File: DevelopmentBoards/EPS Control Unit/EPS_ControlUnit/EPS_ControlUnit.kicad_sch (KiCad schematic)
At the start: 30 parts, among them J1 Conn_01x04_Pin, J2 USB_B_Micro, SW1 SW_SPDT, U1 STM32L476VET6, U2 AMS1117-3.3, Y1 32MHz

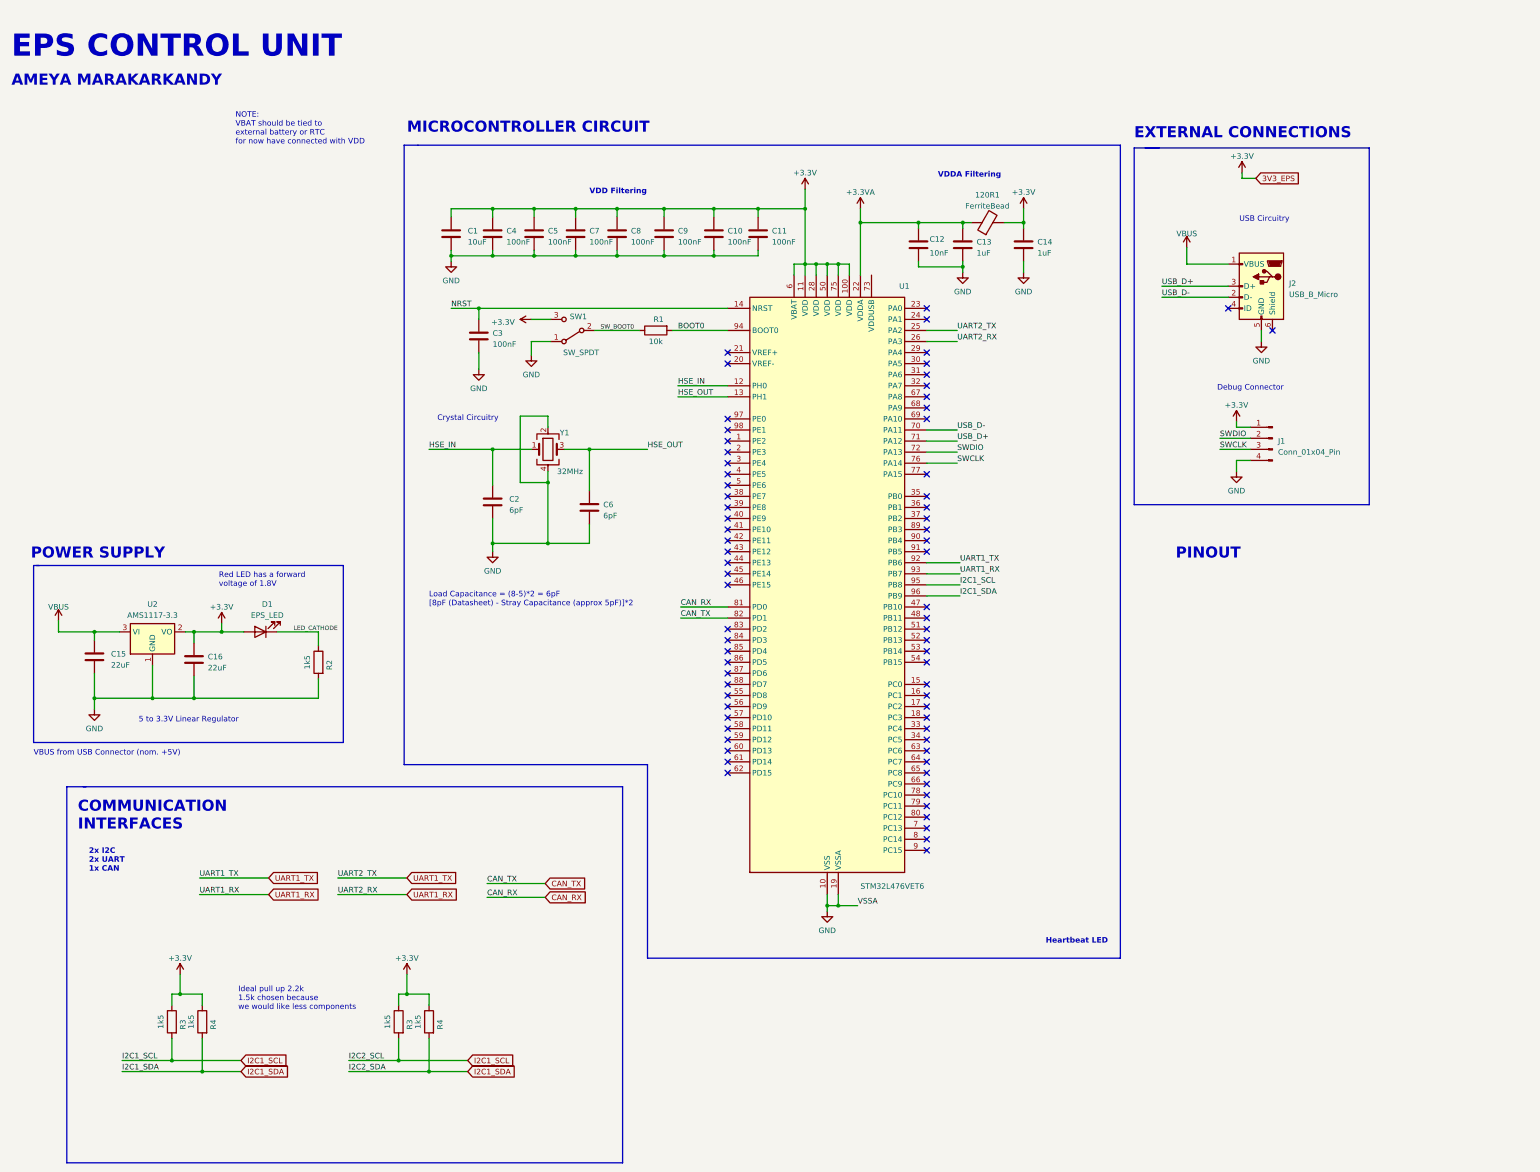
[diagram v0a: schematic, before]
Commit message: EPS Control Unit Dev Board development
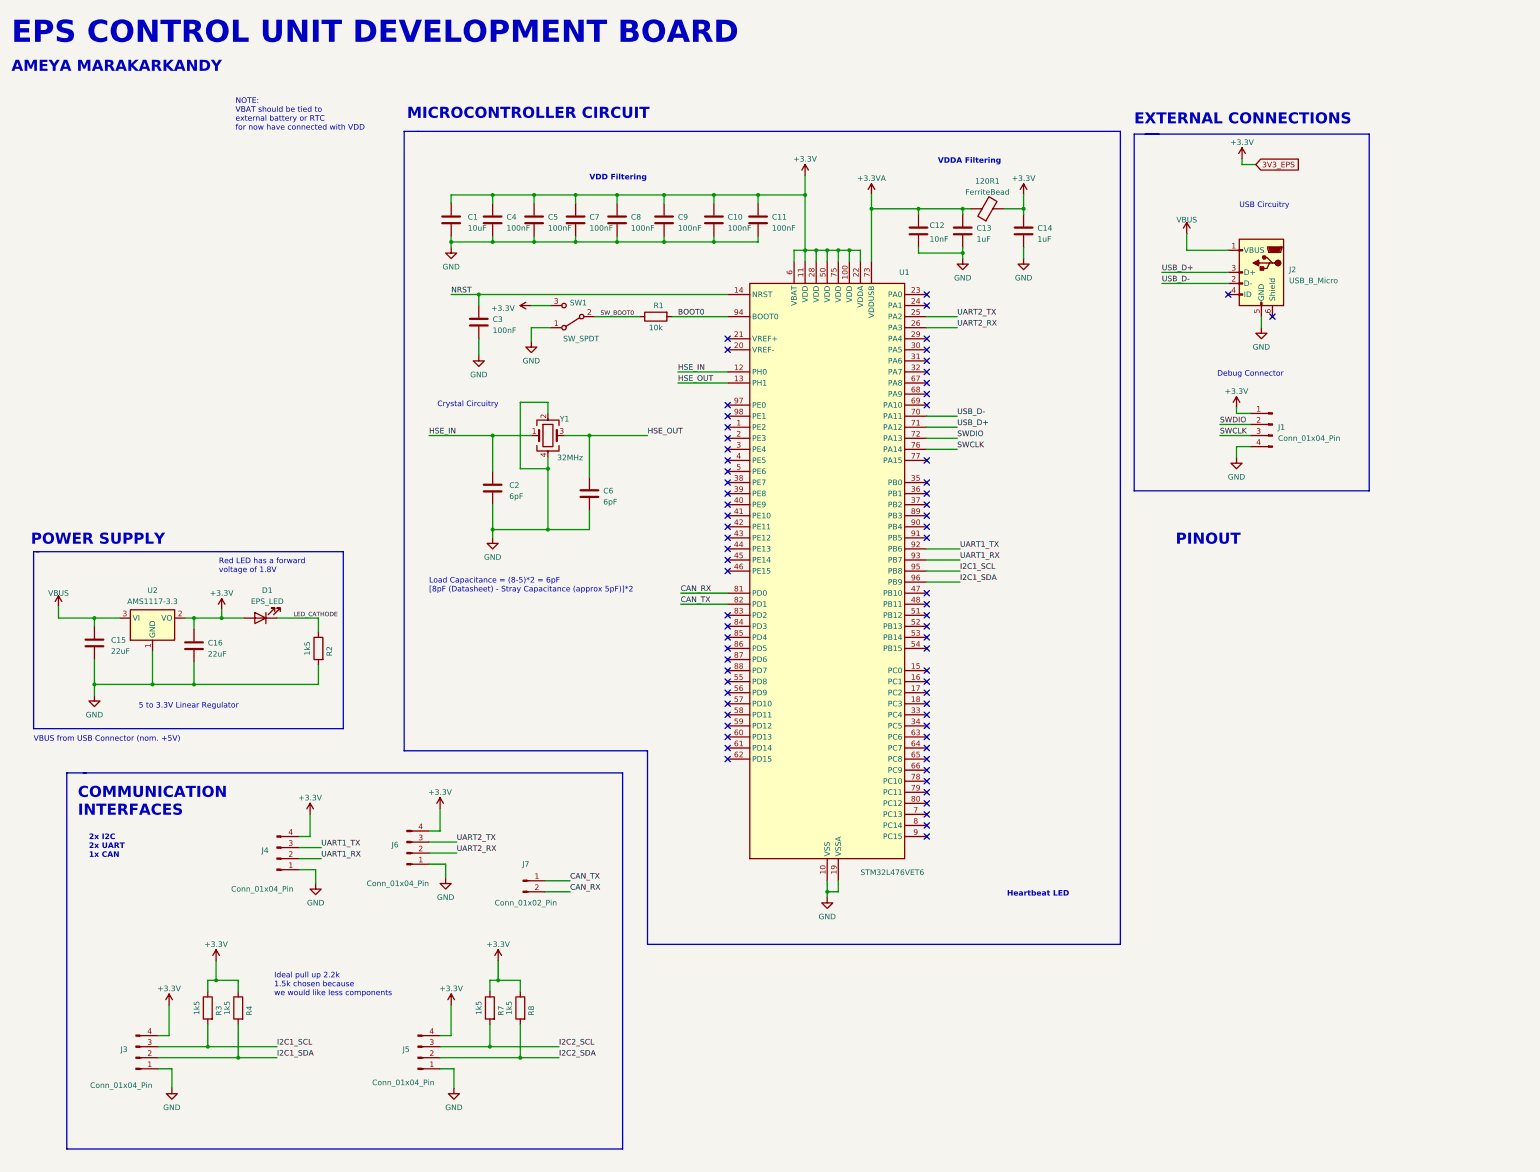
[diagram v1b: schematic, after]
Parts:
- removed R3 (x2), R4 (x2): 1k5, symbol Device:R
- added J3, J4, J5, J6: Conn_01x04_Pin, symbol Connector:Conn_01x04_Pin
- added J7: Conn_01x02_Pin, symbol Connector:Conn_01x02_Pin
- added R3, R4, R7, R8: 1k5, symbol Device:R
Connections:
- net +3.3V: now also U1.22 (VDDA), J3.4 (Pin_4), J4.4 (Pin_4), J5.4 (Pin_4), J6.4 (Pin_4), R3.1, R4.1, R7.1, R8.1
- net +3.3VA: now also U1.73 (VDDUSB); no longer U1.22 (VDDA)
- net CAN_RX: now also J7.2 (Pin_2)
- net CAN_TX: now also J7.1 (Pin_1)
- net GND: now also J3.1 (Pin_1), J4.1 (Pin_1), J5.1 (Pin_1), J6.1 (Pin_1)
- net I2C1_SCL: now also J3.3 (Pin_3), R3.2
- net I2C1_SDA: now also J3.2 (Pin_2), R4.2
- net UART1_RX: now also J4.2 (Pin_2); no longer U1.26 (PA3)
- net UART1_TX: now also J4.3 (Pin_3); no longer U1.25 (PA2)
- new net I2C2_SCL: J5.3 (Pin_3), R7.2
- new net I2C2_SDA: J5.2 (Pin_2), R8.2
- new net UART2_RX: J6.2 (Pin_2), U1.26 (PA3)
- new net UART2_TX: J6.3 (Pin_3), U1.25 (PA2)
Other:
- note added: "EPS CONTROL UNIT DEVELOPMENT BOARD"
- note removed: "EPS CONTROL UNIT"
- company: IIT Bombay Student Satellite Program -> IIT BOMBAY STUDENT SATELLITE PROGRAM
- title: EPS Control Unit -> EPS CONTROL UNIT DEV BOARD

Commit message: EPS Control Unit Rough layout done
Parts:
- added H1, H2, H3, H4: MountingHole_Pad, MountingHole:MountingHole_2.2mm_M2_Pad, symbol Mechanical:MountingHole_Pad
- added JP1, JP2: Jumper_2_Bridged, TestPoint:TestPoint_2Pads_Pitch2.54mm_Drill0.8mm, symbol Jumper:Jumper_2_Bridged
- added TP1, TP3, TP5, TP7, TP9: TestPoint, TestPoint:TestPoint_Pad_D1.0mm, symbol Connector:TestPoint
- added TP2, TP4, TP6, TP8: TestPoint, TestPoint:TestPoint_Pad_1.0x1.0mm, symbol Connector:TestPoint
- added U3: TPS3824-33QDBVRQ1, TPS3824:tps3824, symbol TPS3824:TPS3824-33QDBVRQ1
- 120R1: footprint (none) -> Inductor_SMD:L_0805_2012Metric
- C1, C10, C11, C12, C13, C14, C15, C16, C3, C4, C5, C7, C8, C9: footprint (none) -> Capacitor_SMD:C_0603_1608Metric
- C2, C6: value 6pF -> 10pF; footprint (none) -> Capacitor_SMD:C_0603_1608Metric
- D1: footprint (none) -> LED_SMD:LED_0805_2012Metric
- J1: footprint (none) -> Connector_PinHeader_2.54mm:PinHeader_1x04_P2.54mm_Vertical
- J2: footprint (none) -> Connector_USB:USB_Micro-B_GCT_USB3076-30-A
- J3, J4, J5, J6: footprint (none) -> Connector_PinSocket_2.54mm:PinSocket_1x04_P2.54mm_Vertical
- J7: footprint (none) -> Connector_PinSocket_2.54mm:PinSocket_1x02_P2.54mm_Vertical
- R1, R2, R3, R4, R7, R8: footprint (none) -> Resistor_SMD:R_0805_2012Metric
- SW1: footprint (none) -> Connector_PinHeader_2.54mm:PinHeader_1x03_P2.54mm_Vertical
- Y1: footprint (none) -> Crystal:Crystal_SMD_Abracon_ABM8AIG-4Pin_3.2x2.5mm
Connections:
- net +3.3V: now also U1.73 (VDDUSB), JP2.2 (B), TP7.1, U3.5 (VDD); no longer C16.1, U1.22 (VDDA), U2.2 (VO)
- net +3.3VA: now also U1.22 (VDDA), TP5.1; no longer U1.73 (VDDUSB)
- net GND: now also H1.1, H2.1, H3.1, H4.1, TP2.1, TP4.1, TP6.1, TP8.1, U3.2 (GND)
- net I2C2_SCL: now also U1.47 (PB10)
- net I2C2_SDA: now also U1.48 (PB11)
- net NRST: now also JP1.2 (B), TP9.1
- net VBUS: now also TP1.1
- net WDI: now reaches U1.57 (PD10)
- net WDI: now also U3.4 (WDI)
- new net 3V3_LDO: C16.1, JP2.1 (A), TP3.1, U2.2 (VO)
- new net WDI_RESET: JP1.1 (A), U3.3 (RESET)
- no-connect marks 72 -> 70
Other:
- note added: "Bulk capacitance"
- note added: "Load Capacitance = (10-5)*2 = 10pF [10pF (Datasheet) - Stray Capacitance (approx 5pF)]*2"
- note added: "M2"
- note added: "MOUNTING HOLES"
- note added: "REMINDER TO ADD EPS LED CONTROLLED BBY GPIO PIN"
- note added: "WATCHDOG TIMER"
- note removed: "Load Capacitance = (8-5)*2 = 6pF [8pF (Datasheet) - Stray Capacitance (approx 5pF)]*2"
- moved on the sheet: 120R1, C1, C10, C11, C12, C13, C14, C15, C16, C2, C3, C4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

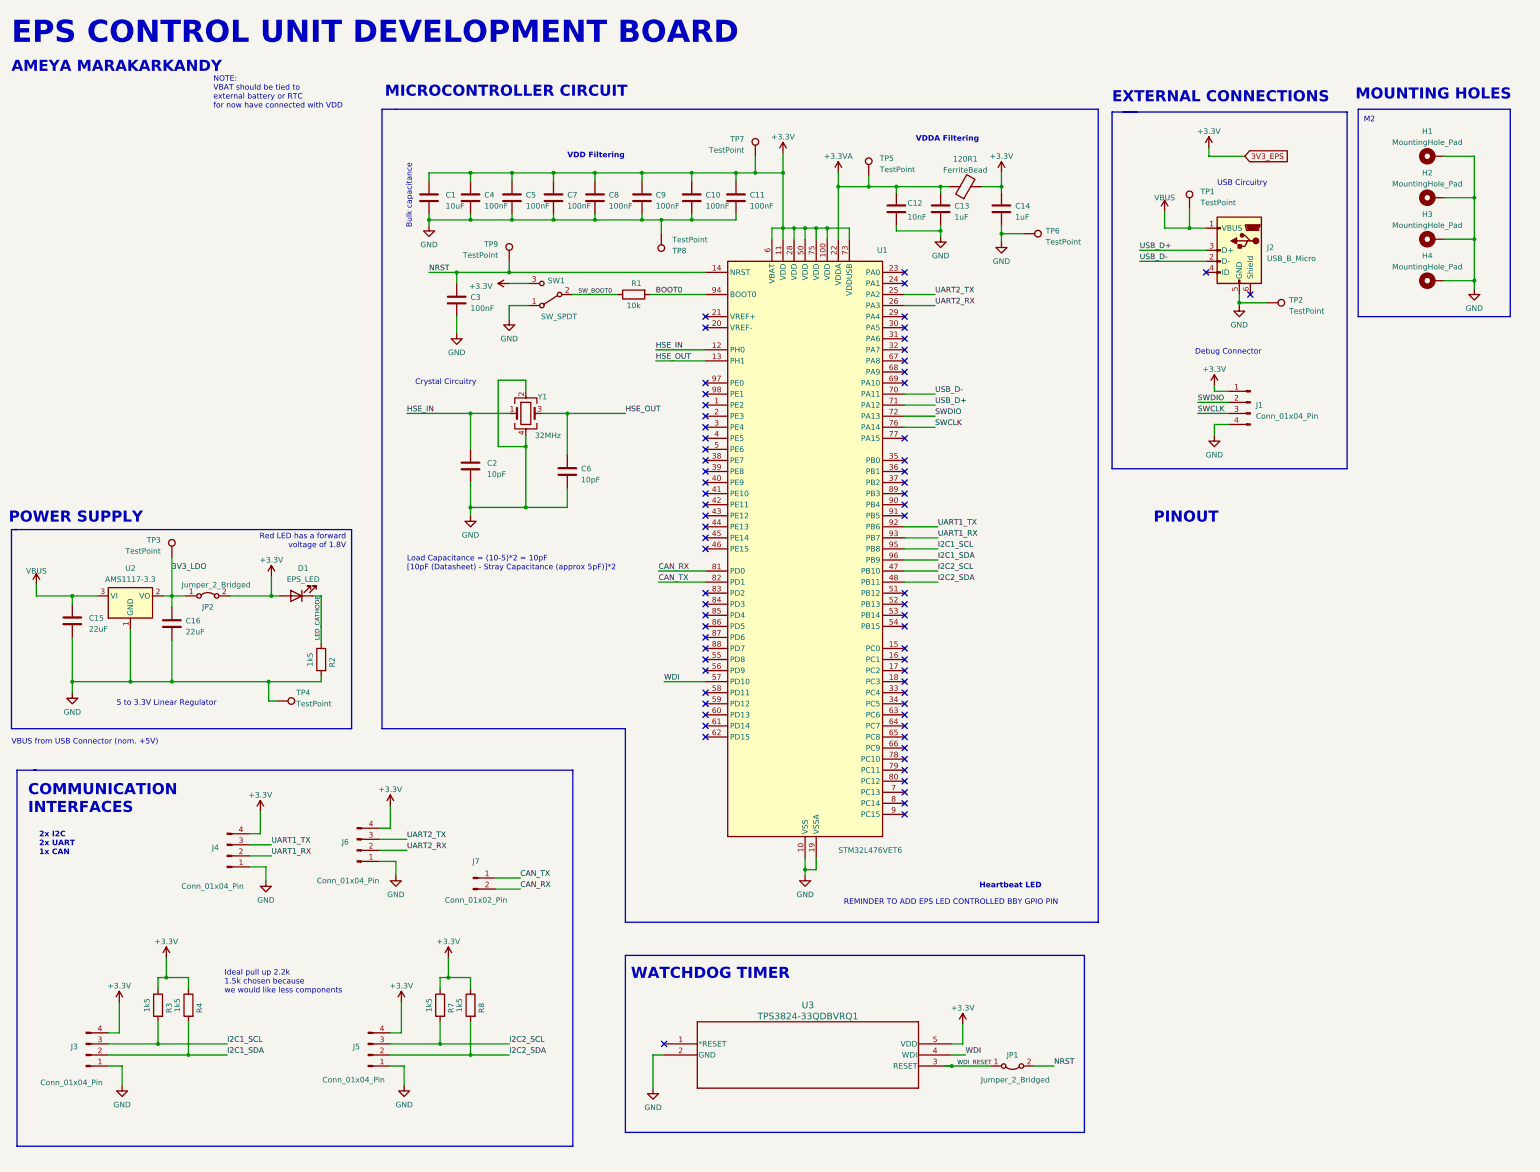
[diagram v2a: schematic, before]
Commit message: EPS Control Unit Dev Board Completed
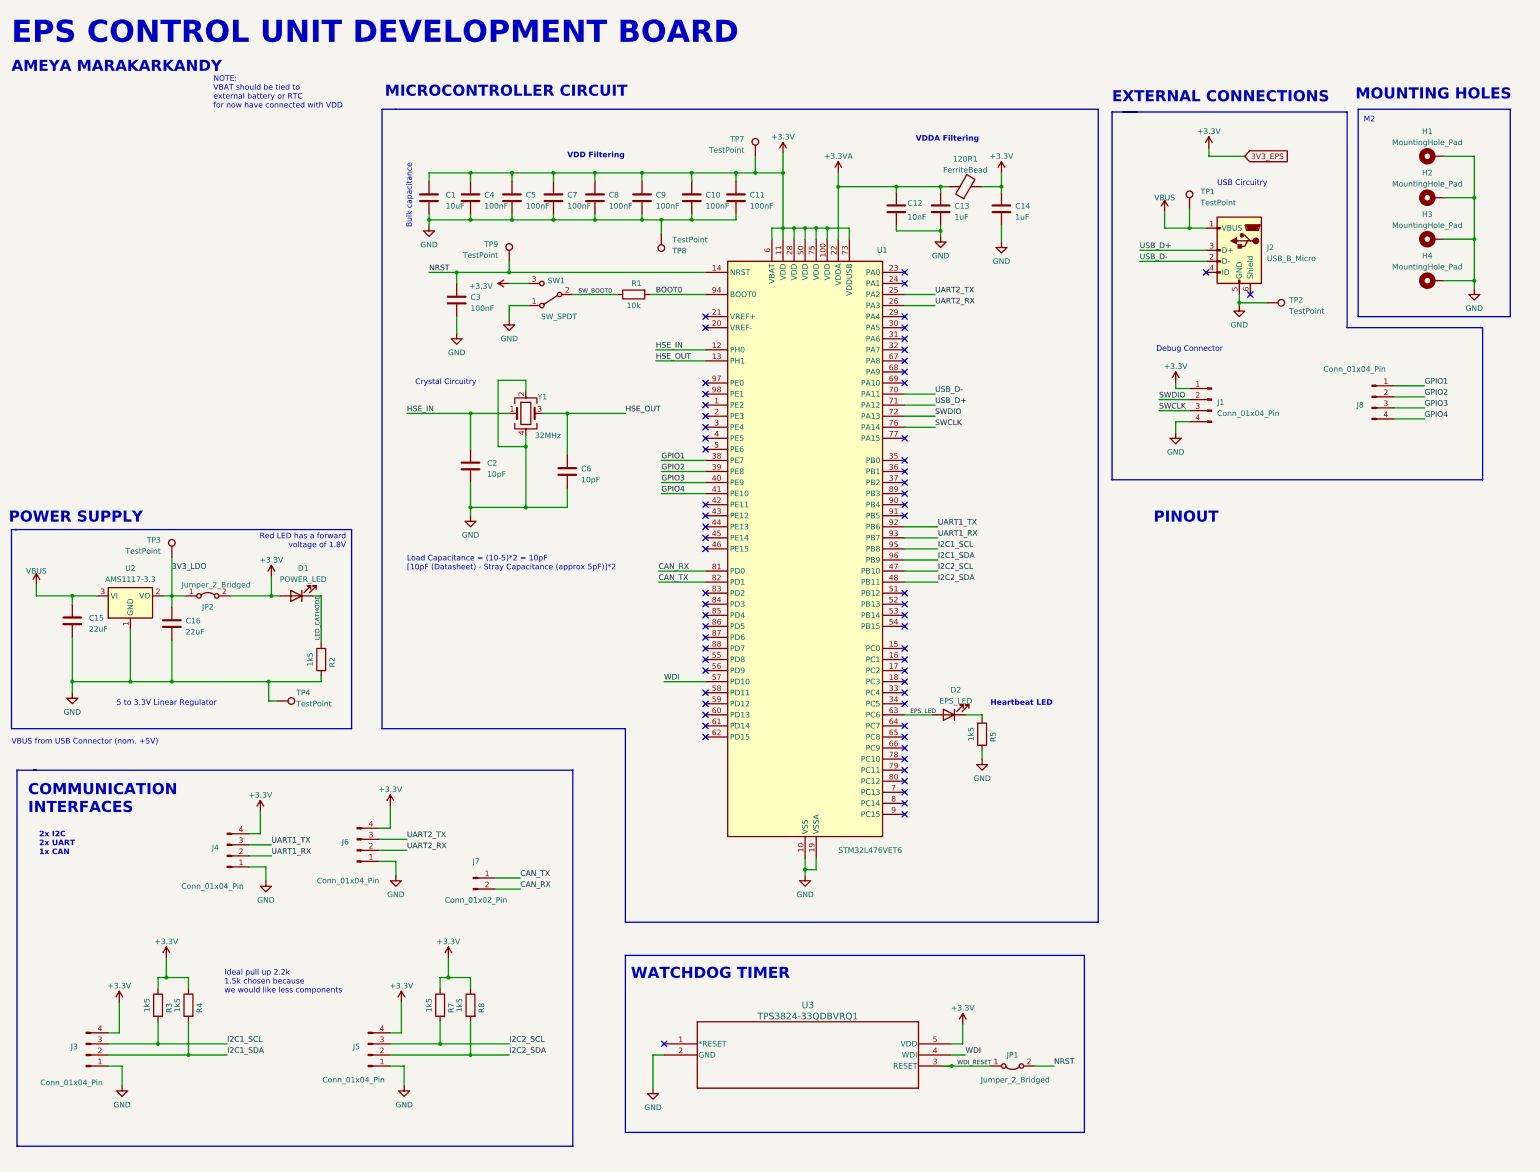
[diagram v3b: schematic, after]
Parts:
- removed TP5: TestPoint, TestPoint:TestPoint_Pad_D1.0mm, symbol Connector:TestPoint
- removed TP6: TestPoint, TestPoint:TestPoint_Pad_1.0x1.0mm, symbol Connector:TestPoint
- added D2: EPS_LED, LED_SMD:LED_0805_2012Metric, symbol Device:LED
- added J8: Conn_01x04_Pin, Connector_PinHeader_2.54mm:PinHeader_1x04_P2.54mm_Vertical, symbol Connector:Conn_01x04_Pin
- added R5: 1k5, Resistor_SMD:R_0805_2012Metric, symbol Device:R
- D1: value EPS_LED -> POWER_LED
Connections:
- net GND: now also R5.2
- net GPIO1: now reaches U1.38 (PE7)
- net GPIO1: now also J8.1 (Pin_1)
- net GPIO2: now reaches U1.39 (PE8)
- net GPIO2: now also J8.2 (Pin_2)
- net GPIO3: now reaches U1.40 (PE9)
- net GPIO3: now also J8.3 (Pin_3)
- net GPIO4: now reaches U1.41 (PE10)
- net GPIO4: now also J8.4 (Pin_4)
- net EPS_LED: now reaches U1.63 (PC6)
- net EPS_LED: now also D2.2 (A)
- new net: D2.1 (K), R5.1
- no-connect marks 70 -> 65
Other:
- note removed: "REMINDER TO ADD EPS LED CONTROLLED BBY GPIO PIN"
- moved on the sheet: J1
